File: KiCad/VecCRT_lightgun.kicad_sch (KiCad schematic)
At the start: 6 parts, among them J8 Conn_01x03, K1 SchEin, Q7 2N7000, X1 OPL820-OC

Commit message: lightgun lamp
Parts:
- added D1: LED, symbol Device:LED
- added R1: 2,2k, RG:R4-2, symbol Device:R
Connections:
- net at Q7.G, R35.1, X1.2: now also D1.1 (K)
- net at J8.1 (Pin_1), R35.2, R36.2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: now also R1.2
- new net: D1.2 (A), R1.1
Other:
- moved on the sheet: J8, K1, Q7, R35, R36, X1

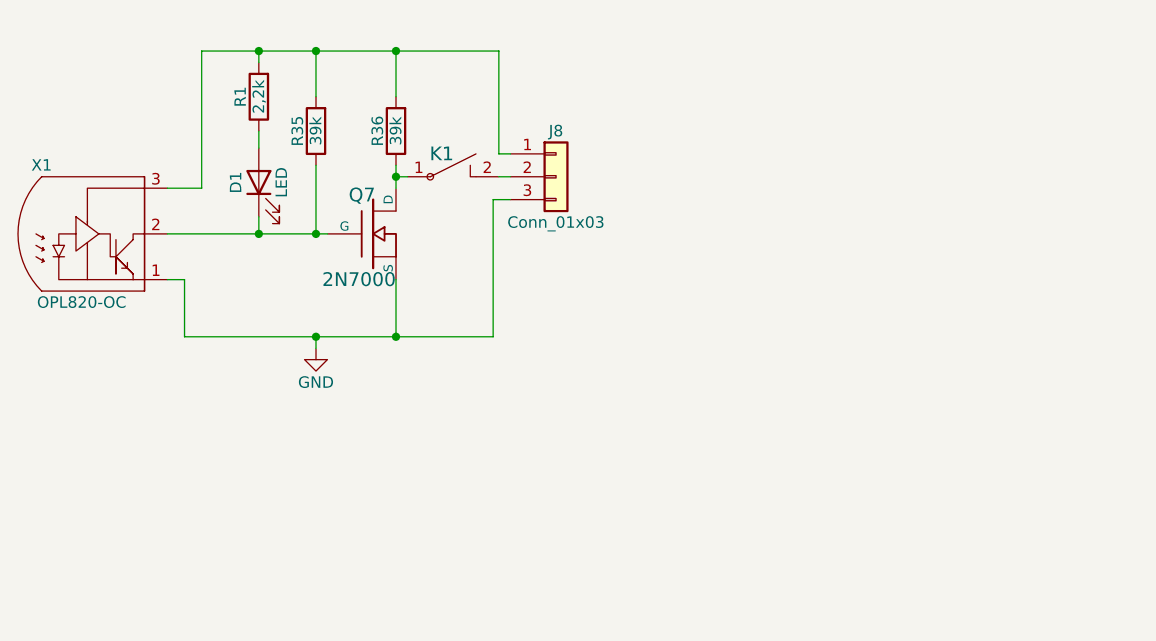
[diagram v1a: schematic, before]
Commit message: Update lightgun LED, add HV, fixes
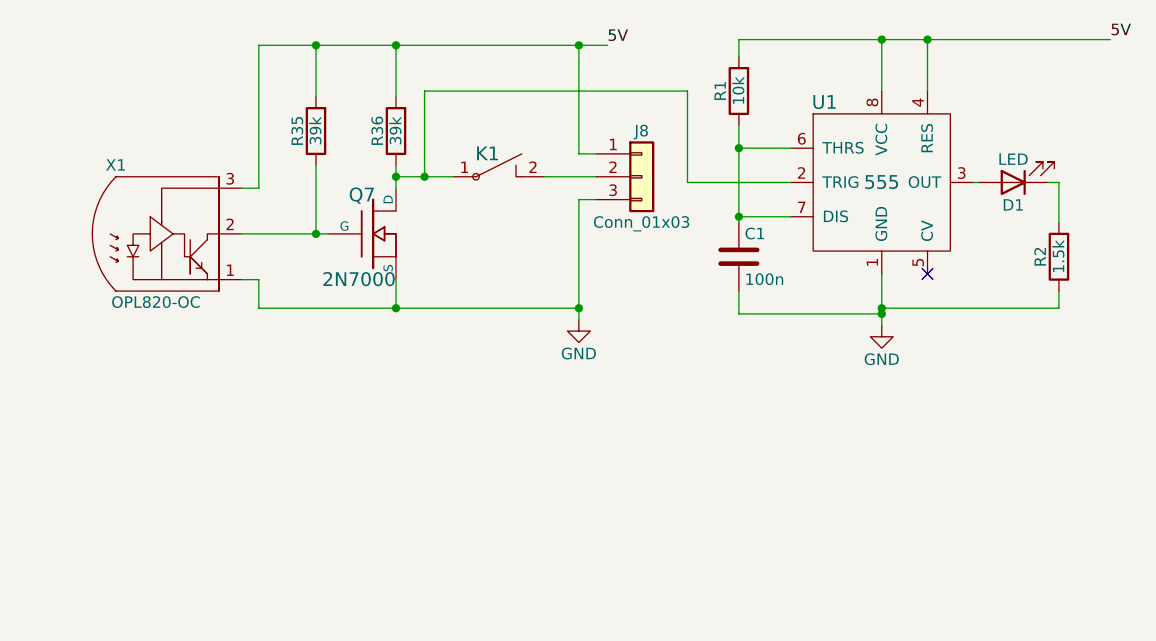
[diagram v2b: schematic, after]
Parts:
- added C1: 100n, RG:C2-2, symbol Device:C
- added R2: 1.5k, RG:R4-2, symbol Device:R
- added U1: 555, RG:DIP-8_300, symbol rg:555
- D1: footprint (none) -> RG:PSS_2W
- J8: footprint RG:PSS_3 -> RG:PSS_3W
- K1: footprint PINHEAD1-2 -> RG:PSS_2W
- R1: value 2,2k -> 10k
- X1: footprint (none) -> RG:PSS_3W
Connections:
- net GND: now also C1.2, R2.1, U1.1 (GND)
- net at K1.1, Q7.D, R36.1: now also U1.2 (TRIG)
- net at D1.2 (A): now also U1.3 (OUT); no longer R1.1
- net 5V: now reaches J8.1 (Pin_1), R1.2, R35.2, R36.2, X1.3
- net 5V: now also U1.4 (RES), U1.8 (VCC)
- net at Q7.G, R35.1, X1.2: no longer D1.1 (K)
- new net: C1.1, R1.1, U1.6 (THRS), U1.7 (DIS)
- new net: D1.1 (K), R2.2
- no-connect marks 0 -> 1
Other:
- moved on the sheet: J8, K1, X1

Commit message: small fixes
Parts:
- D1, K1: footprint RG:PSS_2W -> RG:Pins_2
- J8, X1: footprint RG:PSS_3W -> RG:Pins_3
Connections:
- net 5V: now also J8.3 (Pin_3); no longer J8.1 (Pin_1)
- net GND: now also J8.1 (Pin_1); no longer J8.3 (Pin_3)
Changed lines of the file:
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@@
       (effects (font (size 1.524 1.524)) hide)
     )
-    (property "Footprint" "RG:PSS_2W" (id 2) (at 103.505 54.61 0)
+    (property "Footprint" "RG:Pins_2" (id 2) (at 103.505 54.61 0)
       (effects (font (size 1.524 1.524)) hide)
     )
@@
     (property "Reference" "D1" (id 0) (at 160.02 58.42 0))
     (property "Value" "LED" (id 1) (at 160.02 53.34 0))
-    (property "Footprint" "RG:PSS_2W" (id 2) (at 160.02 55.88 0)
+    (property "Footprint" "RG:Pins_2" (id 2) (at 160.02 55.88 0)
       (effects (font (size 1.27 1.27)) hide)
     )
@@
     (pin "2")
   )
-  (symbol (lib_id "Connector_Generic:Conn_01x03") (at 118.745 55.245 0) (unit 1)
-    (in_bom yes) (on_board yes)
-    (property "Reference" "J8" (id 0) (at 118.745 50.165 0))
-    (property "Value" "Conn_01x03" (id 1) (at 118.745 60.325 0))
-    (property "Footprint" "RG:PSS_3W" (id 2) (at 118.745 55.245 0)
+  (symbol (lib_id "Connector_Generic:Conn_01x03") (at 118.745 55.245 0) (mirror x) (unit 1)
+    (in_bom yes) (on_board yes)
+    (property "Reference" "J8" (id 0) (at 118.745 60.325 0))
+    (property "Value" "Conn_01x03" (id 1) (at 118.745 50.165 0))
+    (property "Footprint" "RG:Pins_3" (id 2) (at 118.745 55.245 0)
       (effects (font (size 1.27 1.27)) hide)
     )
@@
     (property "Reference" "X1" (id 0) (at 60.325 53.975 0))
     (property "Value" "OPL820-OC" (id 1) (at 64.77 69.215 0))
-    (property "Footprint" "RG:PSS_3W" (id 2) (at 70.485 61.595 0)
+    (property "Footprint" "RG:Pins_3" (id 2) (at 70.485 61.595 0)
       (effects (font (size 1.27 1.27)) hide)
     )
@@
     )
     (path "/8f2bca60-b030-4e12-bfb3-a9007d733871"
-      (reference "D1") (unit 1) (value "LED") (footprint "RG:PSS_2W")
+      (reference "D1") (unit 1) (value "LED") (footprint "RG:Pins_2")
     )
     (path "/9bded999-dd68-4925-b69f-7b9b11e93435"
-      (reference "J8") (unit 1) (value "Conn_01x03") (footprint "RG:PSS_3W")
+      (reference "J8") (unit 1) (value "Conn_01x03") (footprint "RG:Pins_3")
     )
     (path "/091250ce-6821-4ba7-b44f-6b424410169f"
-      (reference "K1") (unit 1) (value "SchEin") (footprint "RG:PSS_2W")
+      (reference "K1") (unit 1) (value "SchEin") (footprint "RG:Pins_2")
     )
     (path "/ce1780dd-ef77-4641-a0b1-953ff49d10e9"
@@
     )
     (path "/b647f21c-6cda-445b-a40b-5e53e027d5de"
-      (reference "X1") (unit 1) (value "OPL820-OC") (footprint "RG:PSS_3W")
-    )
-  )
+      (reference "X1") (unit 1) (value "OPL820-OC") (footprint "RG:Pins_3")
+    )
+  )
